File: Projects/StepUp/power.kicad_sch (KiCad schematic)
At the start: 55 parts, among them J10 Conn_01x02, J11 Conn_01x02, J12 Conn_01x02, J13 Conn_01x02, J9 Conn_01x02, Q3 PMF170XP,115, Q4 BSS83P, U5 NCP1117-3.3_SOT223, U6 MCP73832T-2ACI_OT, U7 MIC2253

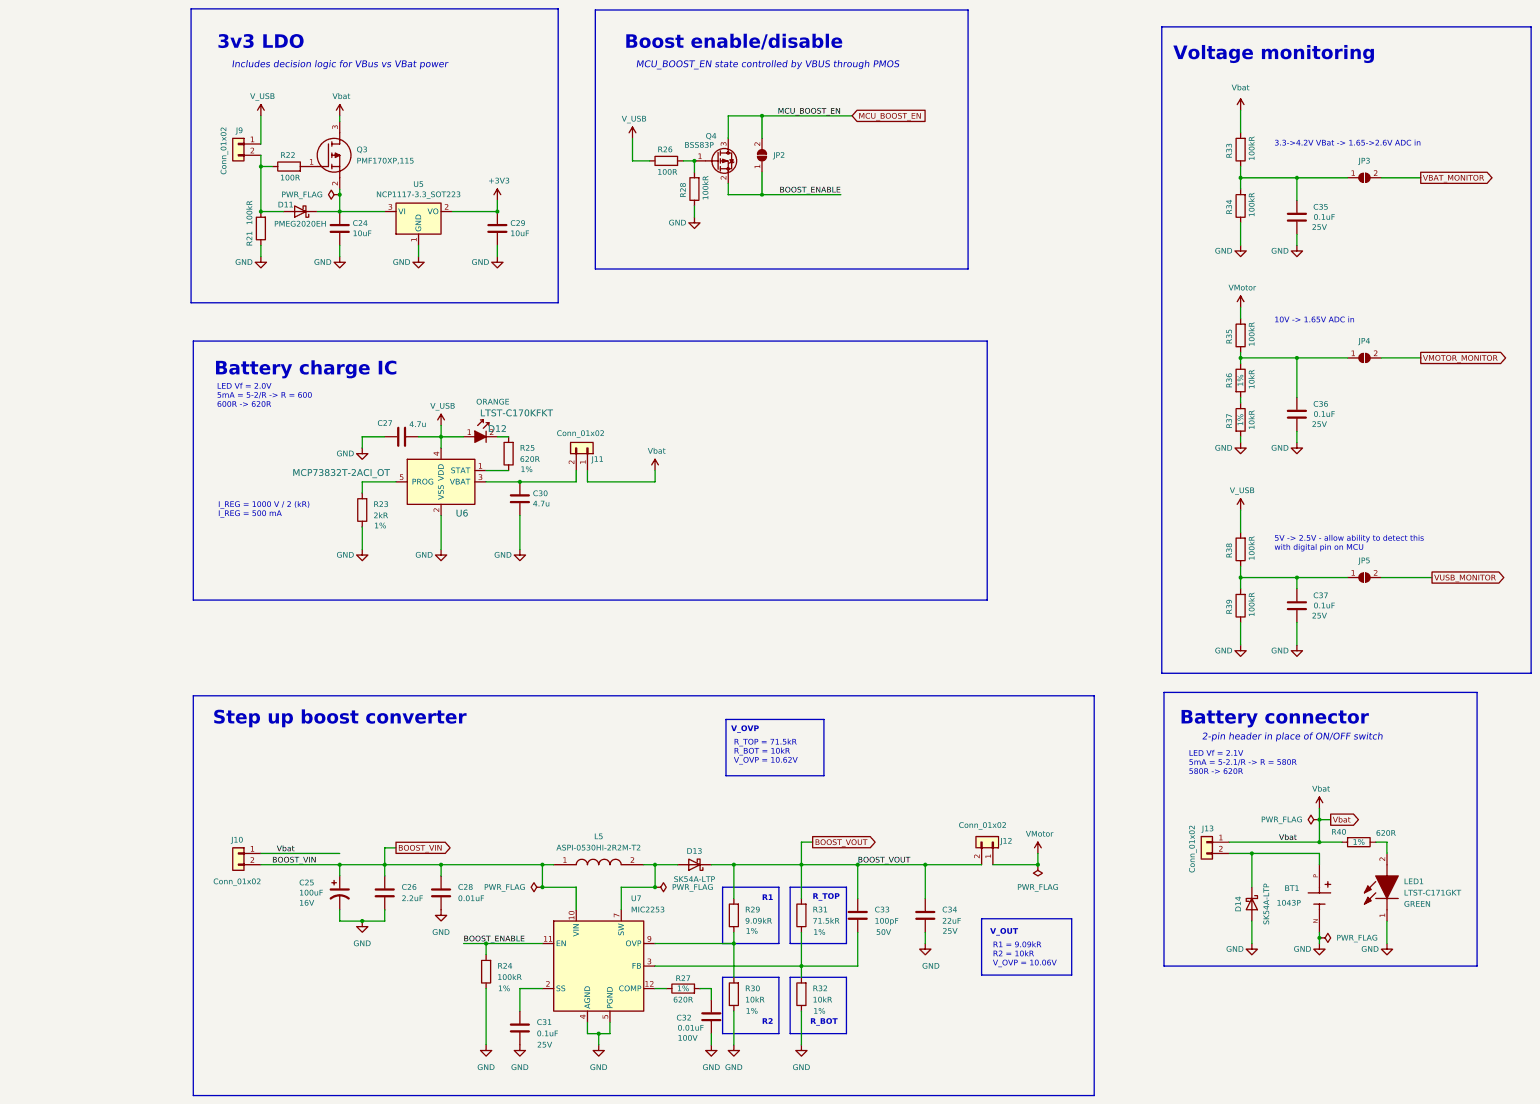
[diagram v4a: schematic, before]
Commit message: feat(layout): DRC ongoing, layout nearly complete
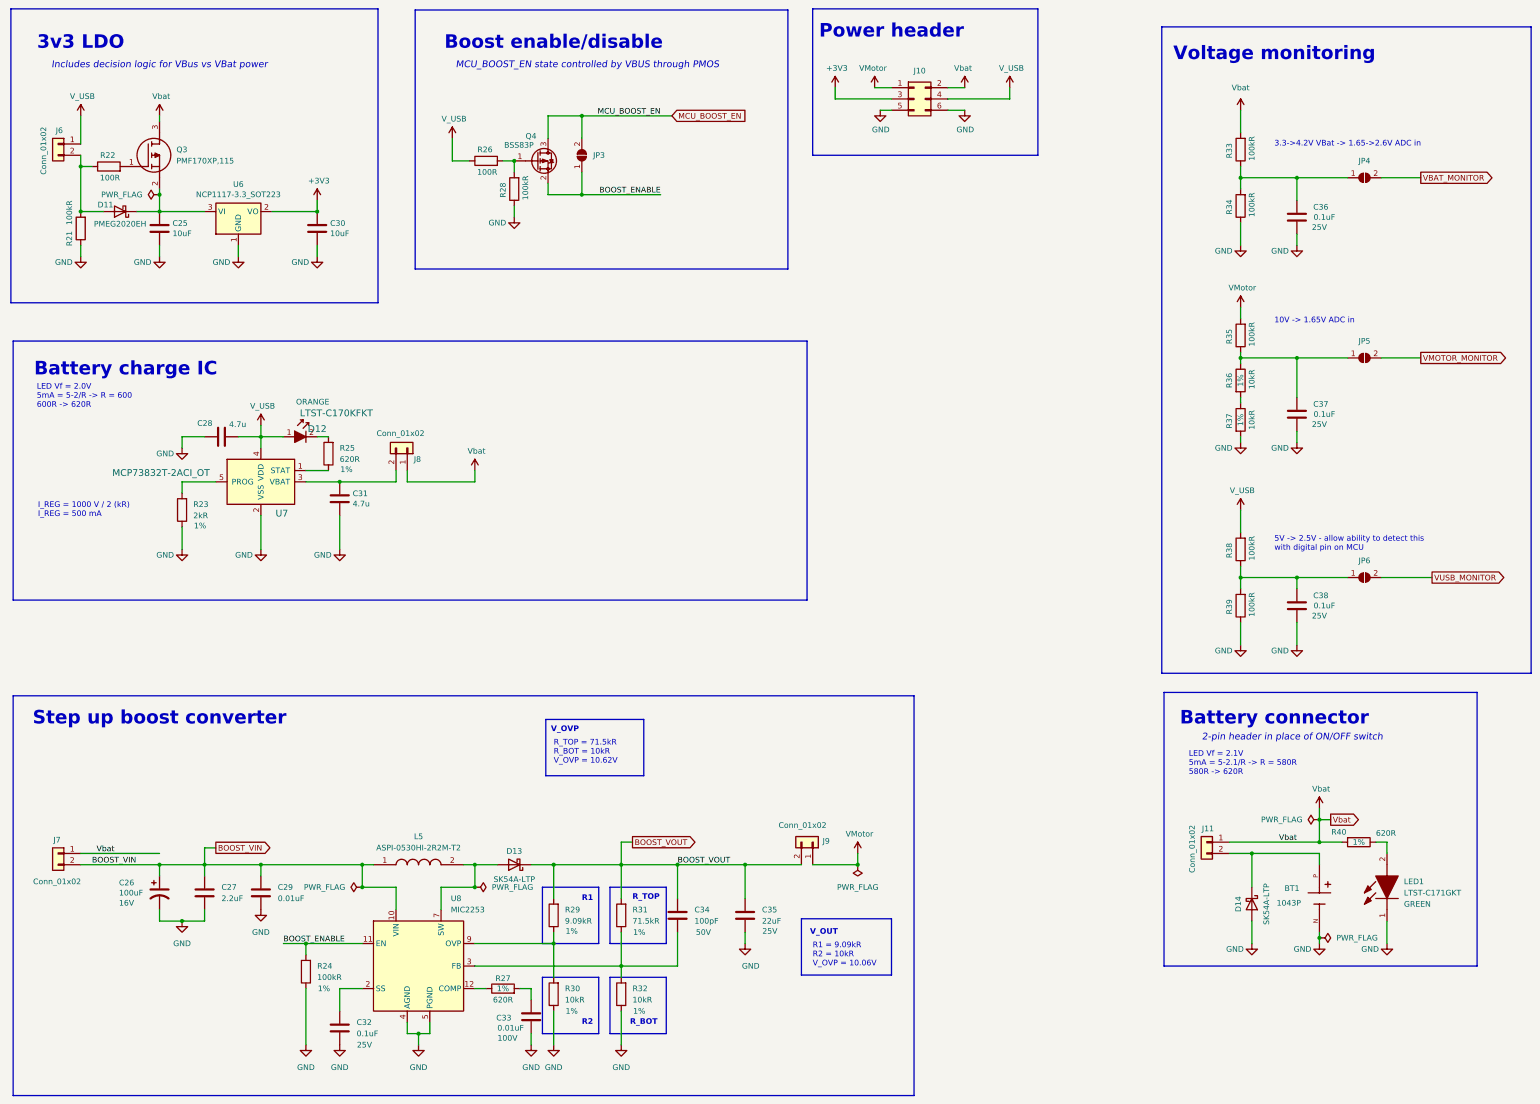
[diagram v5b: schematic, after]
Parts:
- added J10: Conn_02x03_Odd_Even, Connector_PinHeader_2.54mm:PinHeader_2x03_P2.54mm_Vertical, symbol Connector_Generic:Conn_02x03_Odd_Even
- renumbered C24 to C25, C25 to C26, C26 to C27, C27 to C28, C28 to C29, C29 to C30, C30 to C31, C31 to C32, C32 to C33, C33 to C34, C34 to C35, C35 to C36, C36 to C37, C37 to C38, J13 to J11, J9 to J6, J10 to J7, J11 to J8, J12 to J9, JP2 to JP3, JP3 to JP4, JP4 to JP5, JP5 to JP6, U5 to U6, U6 to U7, U7 to U8
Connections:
- net +3V3: now also J10.3 (Pin_3)
- net GND: now also J10.5 (Pin_5), J10.6 (Pin_6)
- net VMotor: now also J10.1 (Pin_1)
- net V_USB: now also J10.4 (Pin_4)
- net Vbat: now also J10.2 (Pin_2)
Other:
- note added: "Power header"
- moved on the sheet: C25, C26, C27, C28, C29, C30, C31, C32, C33, C34, C35, D11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

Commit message: feat(StepUp): Release v0.1
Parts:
- BT1: MPN (none) -> 1043P; Manufacturer (none) -> Keystone Electronics
- C25: value 10uF -> 1uF; Package (none) -> 0805; Type (none) -> SMD; Voltage (none) -> 25V
- C26: MPN (none) -> T491B107M010AT; Manufacturer (none) -> KEMET; Package (none) -> 1411 (3528 Metric); Tolerance (none) -> 20%; Type (none) -> SMD; Voltage 16V -> 10V
- C27, C32, C34, C36, C37, C38: Package (none) -> 0603; Type (none) -> SMD
- C28: value 4.7u -> 4.7uF; Package (none) -> 0805; Type (none) -> SMD
- C29: Package (none) -> 0603; Type (none) -> SMD; Voltage (none) -> 25V
- C30: Package (none) -> 0805; Type (none) -> SMD; Voltage (none) -> 25V
- C31: value 4.7u -> 4.7uF; Package (none) -> 0805; Type (none) -> SMD; Voltage (none) -> 16V
- C33: Package (none) -> 0603; Type (none) -> SMD; Voltage 100V -> 25V
- C35: Package (none) -> 0805; Type (none) -> SMD
- D11: MPN (none) -> PMEG2020EH; Manufacturer (none) -> Generic, none specified; Type (none) -> SMD
- D12, U7: Type (none) -> SMD
- D13, D14: Manufacturer (none) -> Nexperia USA Inc.; Type (none) -> SMD
- J10, J11, J6, J7, J8, J9, JP3, JP4, JP5, JP6: now not fitted
- L5: MPN (none) -> ASPI-0530HI-2R2M-T2; Manufacturer (none) -> Abracon LLC; Type (none) -> SMD
- LED1: MPN (none) -> LTST-C171GKT; Manufacturer (none) -> Lite-On Inc.; Type (none) -> SMD
- Q3: MPN (none) -> PMF170XP,115; Manufacturer (none) -> Nexperia USA Inc.; Type (none) -> SMD
- Q4: MPN (none) -> BSS83PH6327XTSA1; Manufacturer (none) -> Infineon Technologies; Type (none) -> SMD
- R23: renamed from R21; Package (none) -> 0603; Tolerance (none) -> 1%; Type (none) -> SMD
- R24: renamed from R22; Package (none) -> 0603; Tolerance (none) -> 1%; Type (none) -> SMD
- R25: renamed from R23; Package (none) -> 0603; Type (none) -> SMD
- R26: renamed from R24; Package (none) -> 0603; Type (none) -> SMD
- R27: renamed from R25; Package (none) -> 0603; Type (none) -> SMD
- R28: renamed from R26; Package (none) -> 0603; Tolerance (none) -> 1%; Type (none) -> SMD
- R29: renamed from R27; Package (none) -> 0603; Type (none) -> SMD
- R30: renamed from R28; Package (none) -> 0603; Tolerance (none) -> 1%; Type (none) -> SMD
- R31: renamed from R29; Package (none) -> 0603; Type (none) -> SMD
- R32: renamed from R30; Package (none) -> 0603; Type (none) -> SMD
- R33: renamed from R31; Package (none) -> 0603; Type (none) -> SMD
- R34: renamed from R32; Package (none) -> 0603; Type (none) -> SMD
- R35: renamed from R33; Package (none) -> 0603; Tolerance (none) -> 1%; Type (none) -> SMD
- R36: renamed from R34; Package (none) -> 0603; Tolerance (none) -> 1%; Type (none) -> SMD
- R37: renamed from R35; Package (none) -> 0603; Tolerance (none) -> 1%; Type (none) -> SMD
- R38: renamed from R36; Package (none) -> 0603; Type (none) -> SMD
- R39: renamed from R37; Package (none) -> 0603; Type (none) -> SMD
- R40: renamed from R38; Package (none) -> 0603; Tolerance (none) -> 1%; Type (none) -> SMD
- R41: renamed from R39; Package (none) -> 0603; Tolerance (none) -> 1%; Type (none) -> SMD
- R42: renamed from R40; Package (none) -> 0603; Type (none) -> SMD
- U6: value NCP1117-3.3_SOT223 -> LDL1117S33R; MPN (none) -> LDL1117S33R; Manufacturer (none) -> STMicroelectronics; Type (none) -> SMD
- U8: MF (none) -> Microchip; MPN (none) -> MIC2253-06YML-TR; Manufacturer (none) -> Microchip Technology; Type (none) -> SMD
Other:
- company: Samio -> SJFOM

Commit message: feat(BoM): Updating PN's
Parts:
- C25: MPN (none) -> CL21B105KAFNNNE; Manufacturer (none) -> Samsung Electro-Mechanics
- C30: MPN (none) -> GRM21BR61E106KA73K; Manufacturer (none) -> Murata Electronics
- D11: MPN PMEG2020EH -> PMEG2020EH,115; Manufacturer Generic, none specified -> Nexperia
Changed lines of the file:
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@@
 			)
 		)
+		(property "MPN" "GRM21BR61E106KA73K"
+			(at 101.6 72.39 0)
+			(effects
+				(font
+					(size 1.27 1.27)
+				)
+				(hide yes)
+			)
+		)
+		(property "Manufacturer" "Murata Electronics"
+			(at 101.6 72.39 0)
+			(effects
+				(font
+					(size 1.27 1.27)
+				)
+				(hide yes)
+			)
+		)
 		(pin "1"
 		)
@@
 			)
 		)
-		(property "MPN" "PMEG2020EH"
+		(property "MPN" "PMEG2020EH,115"
 			(at 57.15 68.58 0)
 			(effects
@@
 			)
 		)
-		(property "Manufacturer" "Generic, none specified"
+		(property "Manufacturer" "Nexperia"
 			(at 57.15 68.58 0)
 			(effects
@@
 			(at 66.04 72.39 0)
 			(effects
+				(font
+					(size 1.27 1.27)
+				)
+				(hide yes)
+			)
+		)
+		(property "MPN" "CL21B105KAFNNNE"
+			(at 66.04 72.39 0)
+			(effects
+				(font
+					(size 1.27 1.27)
+				)
+				(hide yes)
+			)
+		)
+		(property "Manufacturer" "Samsung Electro-Mechanics"
+			(at 66.04 72.39 0)
+			(effects

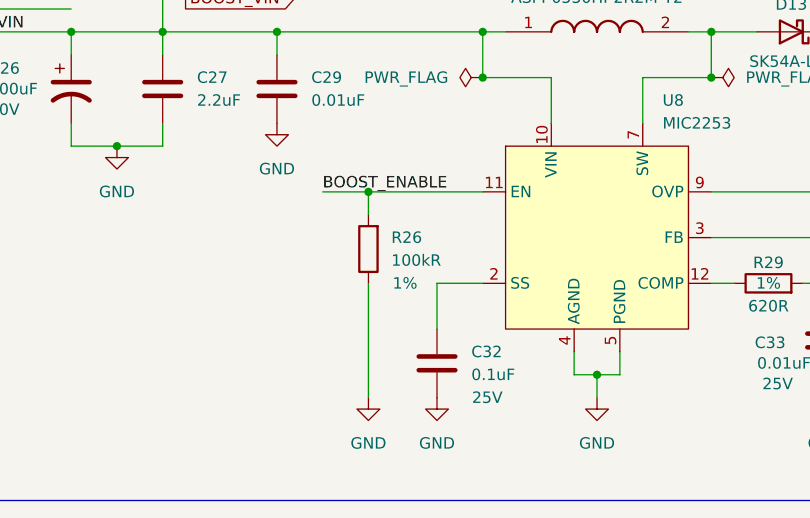
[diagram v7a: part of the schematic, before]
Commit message: chore(bom): Update from PCB BoM
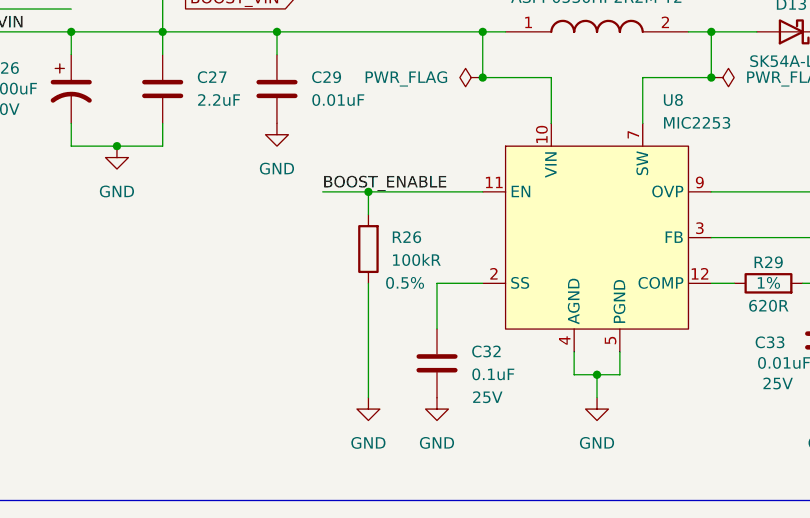
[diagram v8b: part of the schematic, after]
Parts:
- C25: Dielectric (none) -> X7R; Tolerance (none) -> 10%
- C27: Dielectric (none) -> X5R; MPN (none) -> CC0603MRX5R5BB225; Manufacturer (none) -> YAGEO; Tolerance (none) -> 20%; Voltage (none) -> 6.3V
- C28: Dielectric (none) -> X5R; MPN (none) -> CC0805MKX5R6BB475; Manufacturer (none) -> YAGEO; Tolerance (none) -> 20%; Voltage (none) -> 10V
- C29: Dielectric (none) -> X7R; MPN (none) -> CC0603JRX7R8BB103; Manufacturer (none) -> YAGEO; Tolerance (none) -> 5%
- C30: Dielectric (none) -> X5R; Tolerance (none) -> 10%
- C31: Dielectric (none) -> X5R; MPN (none) -> CC0805MKX5R6BB475; Manufacturer (none) -> YAGEO; Tolerance (none) -> 20%; Voltage 16V -> 10V
- C32, C36, C37, C38: Dielectric (none) -> X7R; MPN (none) -> CC0603KRX7R8BB104; Manufacturer (none) -> YAGEO; Tolerance (none) -> 10%
- C33: MPN (none) -> CC0603JRX7R8BB103; Manufacturer (none) -> YAGEO; Tolerance (none) -> 5%
- C34: Dielectric (none) -> C0G, NP0; MPN (none) -> CC0603JRNPO9BN101; Manufacturer (none) -> YAGEO; Tolerance (none) -> 5%
- C35: Dielectric (none) -> X5R; MPN (none) -> CC0805MKX5R8BB226; Manufacturer (none) -> YAGEO; Tolerance (none) -> 20%
- R23, R26, R30, R35, R36, R37, R40, R41: MPN (none) -> RT0603DRE10100KL; Manufacturer (none) -> YAGEO; Power (none) -> 0.1W, 1/10W; Tolerance 1% -> 0.5%
- R24, R28: MPN (none) -> RC0603FR-07100RL; Manufacturer (none) -> YAGEO; Power (none) -> 0.1W, 1/10W
- R25: MPN (none) -> RC0603FR-072KL; Manufacturer (none) -> YAGEO; Power (none) -> 0.1W, 1/10W
- R27, R29, R42: MPN (none) -> RC0603FR-07620RL; Manufacturer (none) -> YAGEO; Power (none) -> 0.1W, 1/10W
- R31: MPN (none) -> RC0603FR-079K09L; Manufacturer (none) -> YAGEO; Power (none) -> 0.1W, 1/10W
- R32, R34, R38, R39: MPN (none) -> RC0603FR-0710KL; Manufacturer (none) -> YAGEO; Power (none) -> 0.1W, 1/10W
- R33: MPN (none) -> RC0603FR-0771K5L; Manufacturer (none) -> YAGEO; Power (none) -> 0.1W, 1/10W
